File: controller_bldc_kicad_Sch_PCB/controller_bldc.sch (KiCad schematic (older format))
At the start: 57 parts, among them J1 Battery Supply, J2 Emergency Button OUT, J3 Emergency Button IN, J4 Brake, J5 Throttle, J6 LM35, J7 Hall Sensors, J8 Nextion Nx3224T028, J9 BLDC Motor, K1 ADW11, Q1 IRF1010N, Q2 IRF1010N, Q3 IRF1010N, Q4 IRF1010N, Q5 IRF1010N, Q6 IRF1010N, SW1 ON_OFF, SW2 OPC, U1 ESP32-DEVKITC-32D, U2 LM317_TO-220, U3 LM7805_TO220, U4 IR2103, U8 IR2103, U9 IR2103

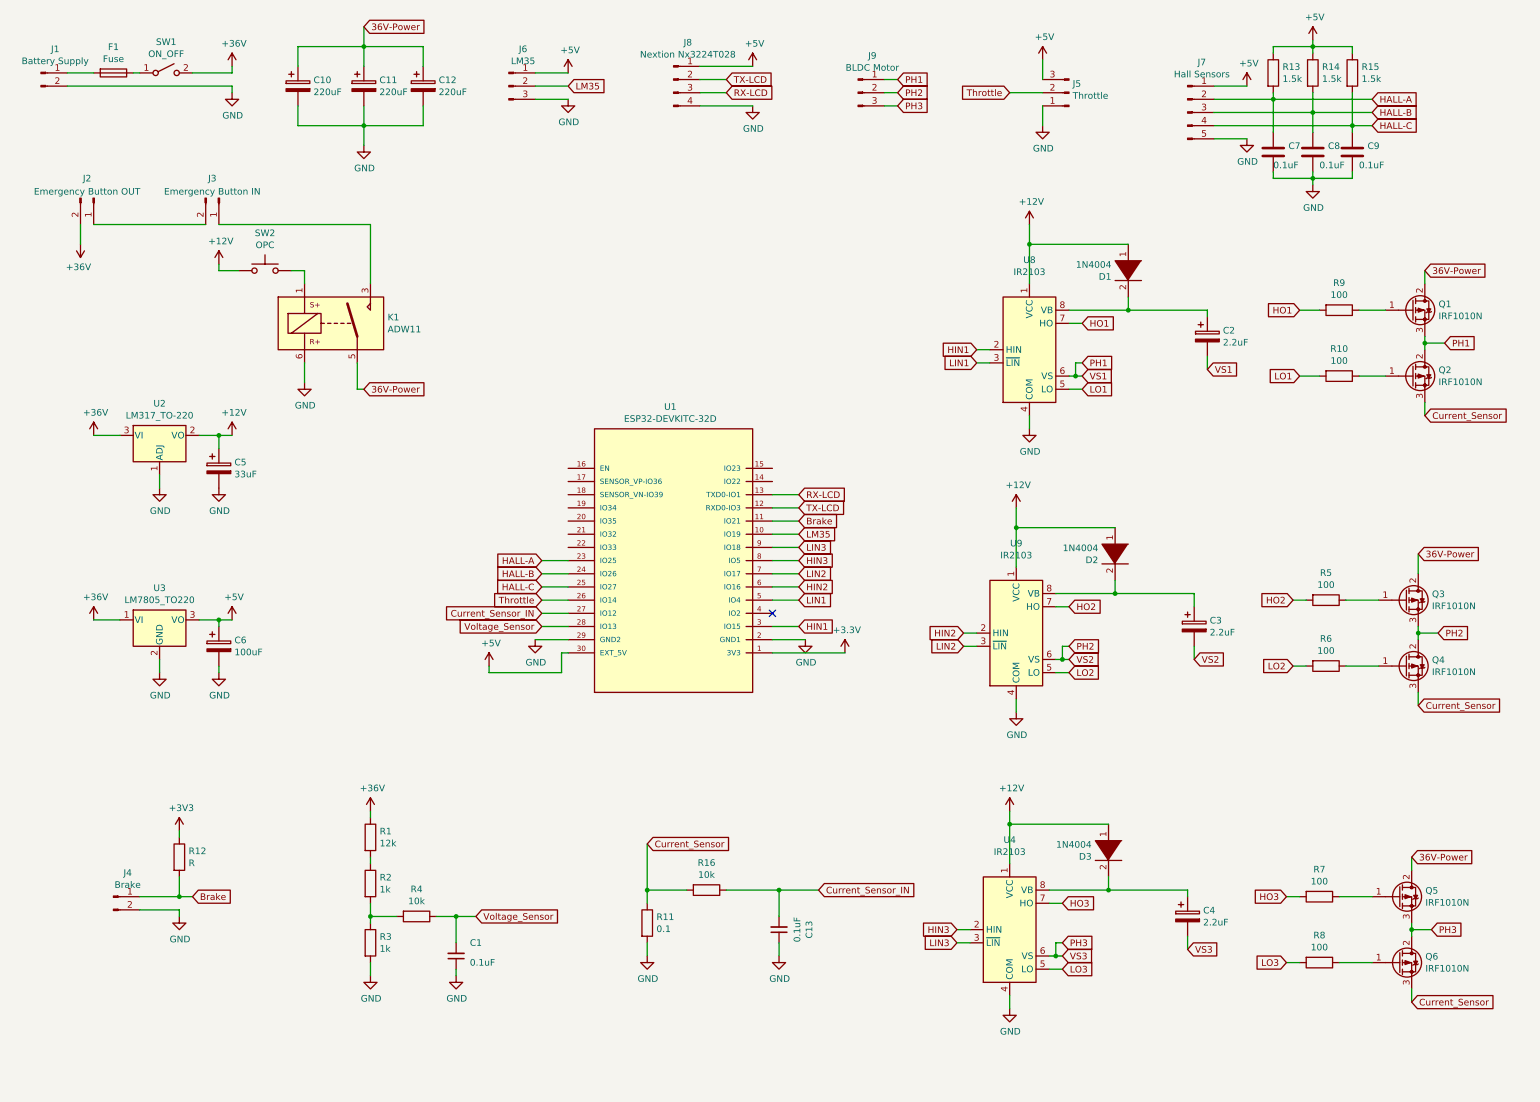
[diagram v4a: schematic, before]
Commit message: PCB: Finished with DC Power Sources and Amp. Op. for sensors
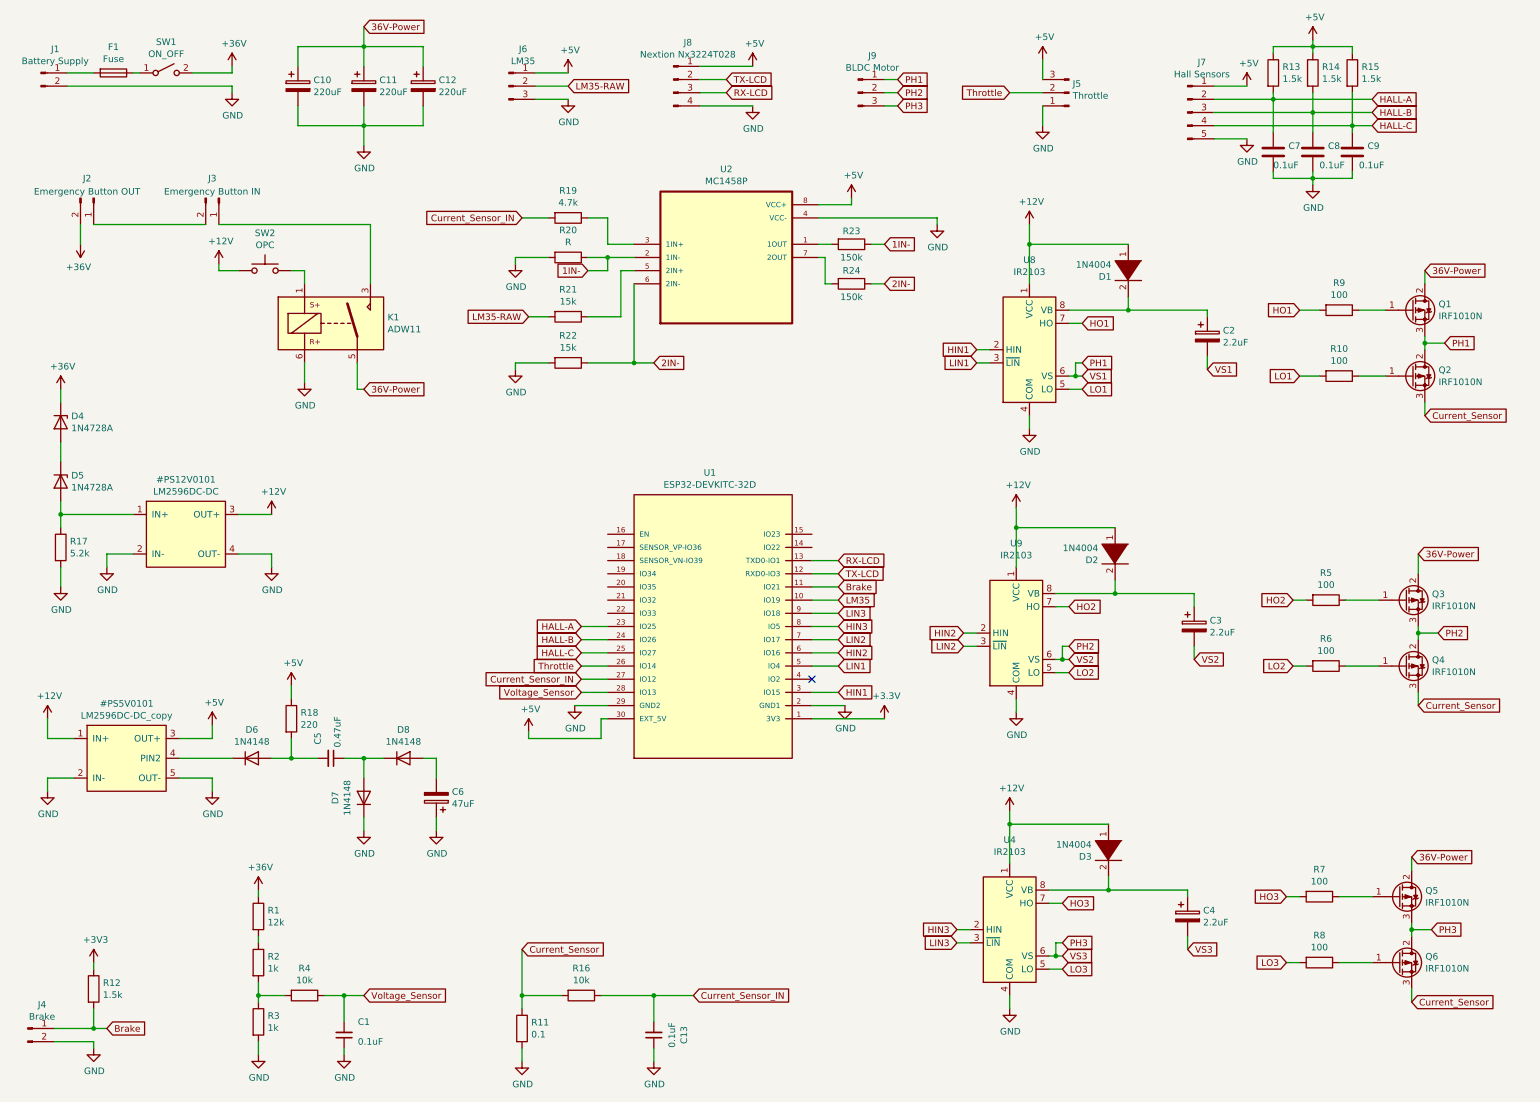
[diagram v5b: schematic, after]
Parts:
- removed C5: 33uF, Capacitor_THT:CP_Radial_D8.0mm_P3.50mm, symbol Device:CP
- removed U2: LM317_TO-220, Package_TO_SOT_THT_Electeam:TO-220-3_Horizontal_TabDown, symbol Regulator_Linear:LM317_TO-220
- removed U3: LM7805_TO220, Package_TO_SOT_THT_Electeam:TO-220-3_Horizontal_TabDown, symbol Regulator_Linear:LM7805_TO220
- added C5: 0.47uF, Capacitor_THT:C_Disc_D7.5mm_W5.0mm_P10.00mm, symbol Device:C_Small
- added D4, D5: 1N4728A, Diode_THT:D_DO-41_SOD81_P10.16mm_Horizontal, symbol Diode:1N47xxA
- added D6, D7, D8: 1N4148, Diode_THT:D_DO-35_SOD27_P7.62mm_Horizontal, symbol Diode:1N4148
- added R17: 5.2k, symbol Device:R
- added R18: 220, symbol Device:R
- added R19: 4.7k, symbol Device:R
- added R20: R, symbol Device:R
- added R21, R22: 15k, symbol Device:R
- added R23, R24: 150k, symbol Device:R
- added U2: MC1458P, DIP794W45P254L959H508Q8, symbol MC1458P:MC1458P
- C6: value 100uF -> 47uF; footprint Capacitor_THT:CP_Radial_D6.3mm_P2.50mm -> (none)
- R12: value R -> 1.5k
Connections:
- net +36V: now also D4.1 (K)
- net +5V: now also R18.1, U2.8 (VCC+); no longer C6.1
- net Current_Sensor_IN: now also R19.2
- net GND: now also C6.1, D7.1 (K), R17.2, R20.2, R22.2, U2.4 (VCC-); no longer C6.2
- net LM35: no longer J6.2 (Pin_2)
- new net: R23.2, U2.1 (1OUT)
- new net: R19.1, U2.3 (1IN+)
- new net: R21.1, U2.5 (2IN+)
- new net: R24.2, U2.7 (2OUT)
- new net: D4.2 (A), D5.1 (K)
- new net: D5.2 (A), R17.1
- new net: C5.1, D7.2 (A), D8.1 (K)
- new net: C6.2, D8.2 (A)
- new net: C5.2, D6.2 (A), R18.2
- new net 1IN-: R20.1, R23.1, U2.2 (1IN-)
- new net 2IN-: R22.1, R24.1, U2.6 (2IN-)
- new net LM35-RAW: J6.2 (Pin_2), R21.2
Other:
- moved on the sheet: C1, C13, J4, R1, R11, R12, R16, R2, R3, R4, U1

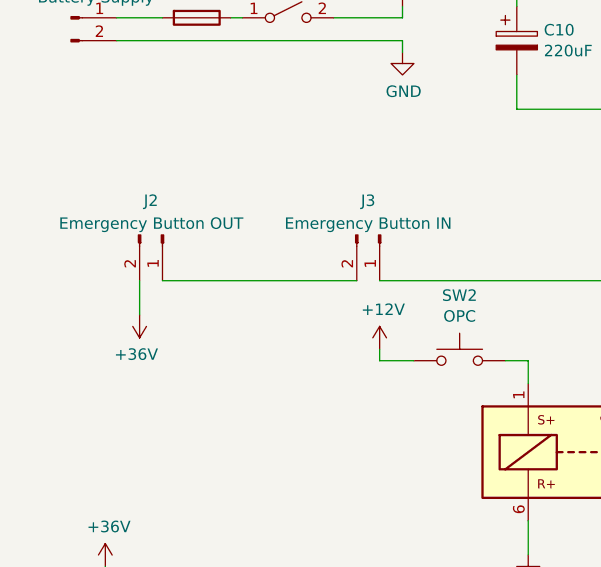
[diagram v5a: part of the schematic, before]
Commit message: PCB: Footprints changed for DC Sources and the OPC realy
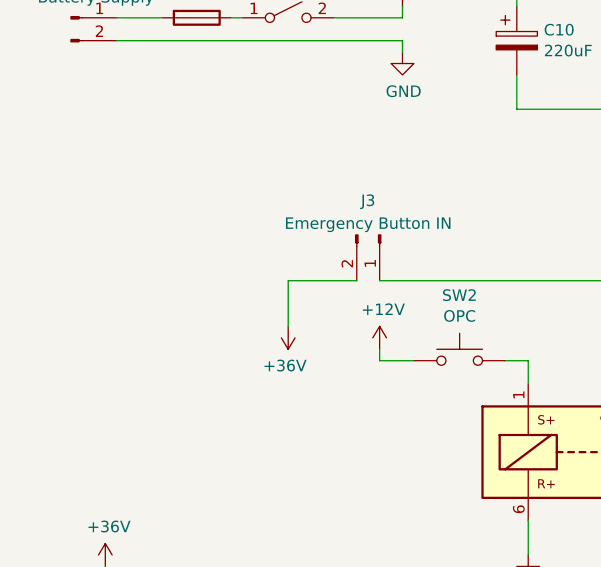
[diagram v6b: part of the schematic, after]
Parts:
- removed J2: Emergency Button OUT, Connector_Phoenix_GMSTB:PhoenixContact_GMSTBA_2,5_2-G_1x02_P7.50mm_Horizontal, symbol Connector:Conn_01x02_Male
- K1: footprint Relay_THT:Relay_1P1T_NO_10x24x18.8mm_Panasonic_ADW11xxxxW_THT -> Relay_THT:Relay_SPDT_RAYEX-L90
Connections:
- net +36V: now also J3.2 (Pin_2)
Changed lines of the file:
@@
 	5350 550  5550 550
-$Comp
-L Connector:Conn_01x02_Male J2
-U 1 1 606A4893
-P 750 1450
-F 0 "J2" V 600 1400 50  0000 C CNN
-F 1 "Emergency Button OUT" V 700 1400 50  0000 C CNN
-F 2 "Connector_Phoenix_GMSTB:PhoenixContact_GMSTBA_2,5_2-G_1x02_P7.50mm_Horizontal" H 750 1450 50  0001 C CNN
-F 3 "~" H 750 1450 50  0001 C CNN
-	1    750  1450
-	0    1    1    0
-$EndComp
 $Comp
 L Connector:Conn_01x02_Male J3
@@
 	0    1    1    0
 $EndComp
-$Comp
-L power:+36V #PWR03
-U 1 1 607E0827
-P 650 1800
-F 0 "#PWR03" H 650 1650 50  0001 C CNN
-F 1 "+36V" H 665 1973 50  0000 C CNN
-F 2 "" H 650 1800 50  0001 C CNN
-F 3 "" H 650 1800 50  0001 C CNN
-	1    650  1800
-	-1   0    0    1
-$EndComp
-Wire Wire Line
-	650  1800 650  1650
-Wire Wire Line
-	750  1650 1600 1650
 Text GLabel 2800 2900 2    50   Input ~ 0
 36V-Power
@@
 F 0 "K1" H 2980 2446 50  0000 L CNN
 F 1 "ADW11" H 2980 2355 50  0000 L CNN
-F 2 "Relay_THT:Relay_1P1T_NO_10x24x18.8mm_Panasonic_ADW11xxxxW_THT" H 3875 2350 50  0001 C CNN
+F 2 "Relay_THT:Relay_SPDT_RAYEX-L90" H 3875 2350 50  0001 C CNN
 F 3 "https://www.panasonic-electric-works.com/pew/es/downloads/ds_dw_hl_en.pdf" H 2550 2400 50  0001 C CNN
 	1    2550 2400
@@
 F 0 "#PS5V0101" H 1000 6115 50  0000 C CNN
 F 1 "LM2596DC-DC_copy" H 1000 6024 50  0000 C CNN
-F 2 "" H 1000 5700 50  0001 C CNN
+F 2 "Package_TO_SOT_THT_Electeam:LM2596DC-DC-HW411" H 1000 5700 50  0001 C CNN
 F 3 "" H 1000 5700 50  0001 C CNN
 	1    1000 5700
@@
 F 0 "#PS12V0101" H 1450 4415 50  0000 C CNN
 F 1 "LM2596DC-DC" H 1450 4324 50  0000 C CNN
-F 2 "" H 1450 4000 50  0001 C CNN
+F 2 "Package_TO_SOT_THT_Electeam:LM2596DC-DC-HW411" H 1450 4000 50  0001 C CNN
 F 3 "" H 1450 4000 50  0001 C CNN
 	1    1450 4000
@@
 Wire Wire Line
 	3950 2700 3950 2750
+$Comp
+L power:+36V #PWR03
+U 1 1 607E0827
+P 1300 1850
+F 0 "#PWR03" H 1300 1700 50  0001 C CNN
+F 1 "+36V" H 1315 2023 50  0000 C CNN
+F 2 "" H 1300 1850 50  0001 C CNN
+F 3 "" H 1300 1850 50  0001 C CNN
+	1    1300 1850
+	-1   0    0    1
+$EndComp
+Wire Wire Line
+	1600 1650 1300 1650
+Wire Wire Line
+	1300 1650 1300 1850
 $EndSCHEMATC

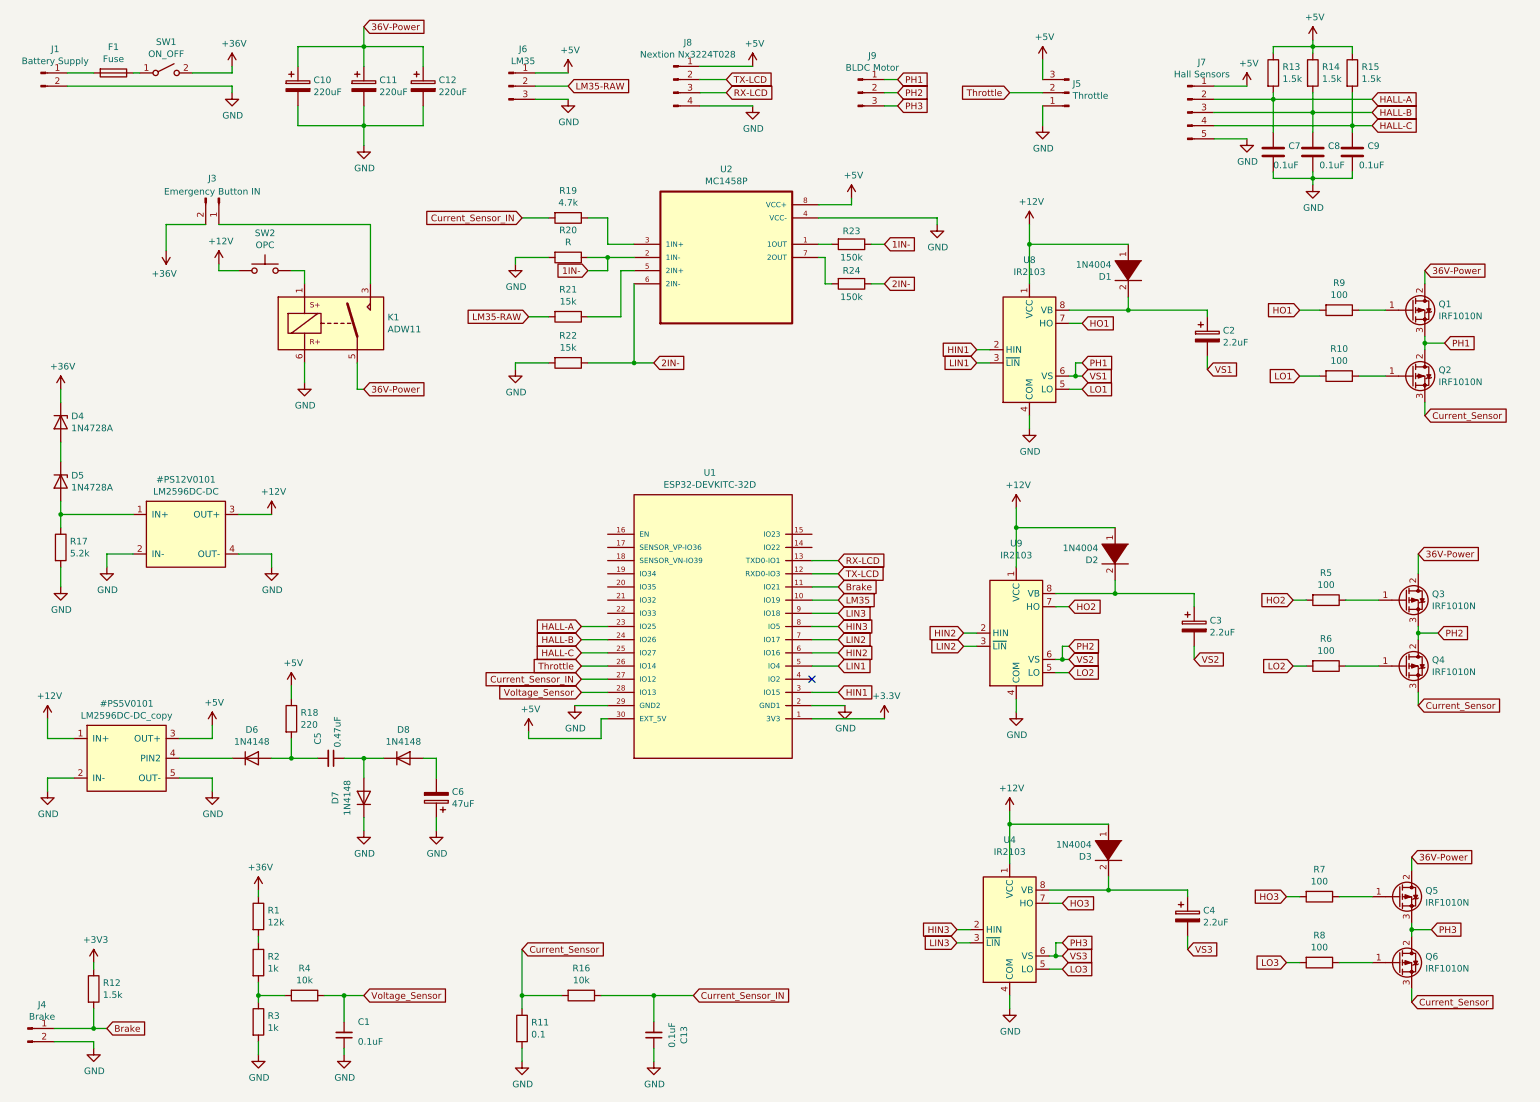
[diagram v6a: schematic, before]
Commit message: This fixes PCB and Schematic, closes #5, closes #6, closes #7, closes #8
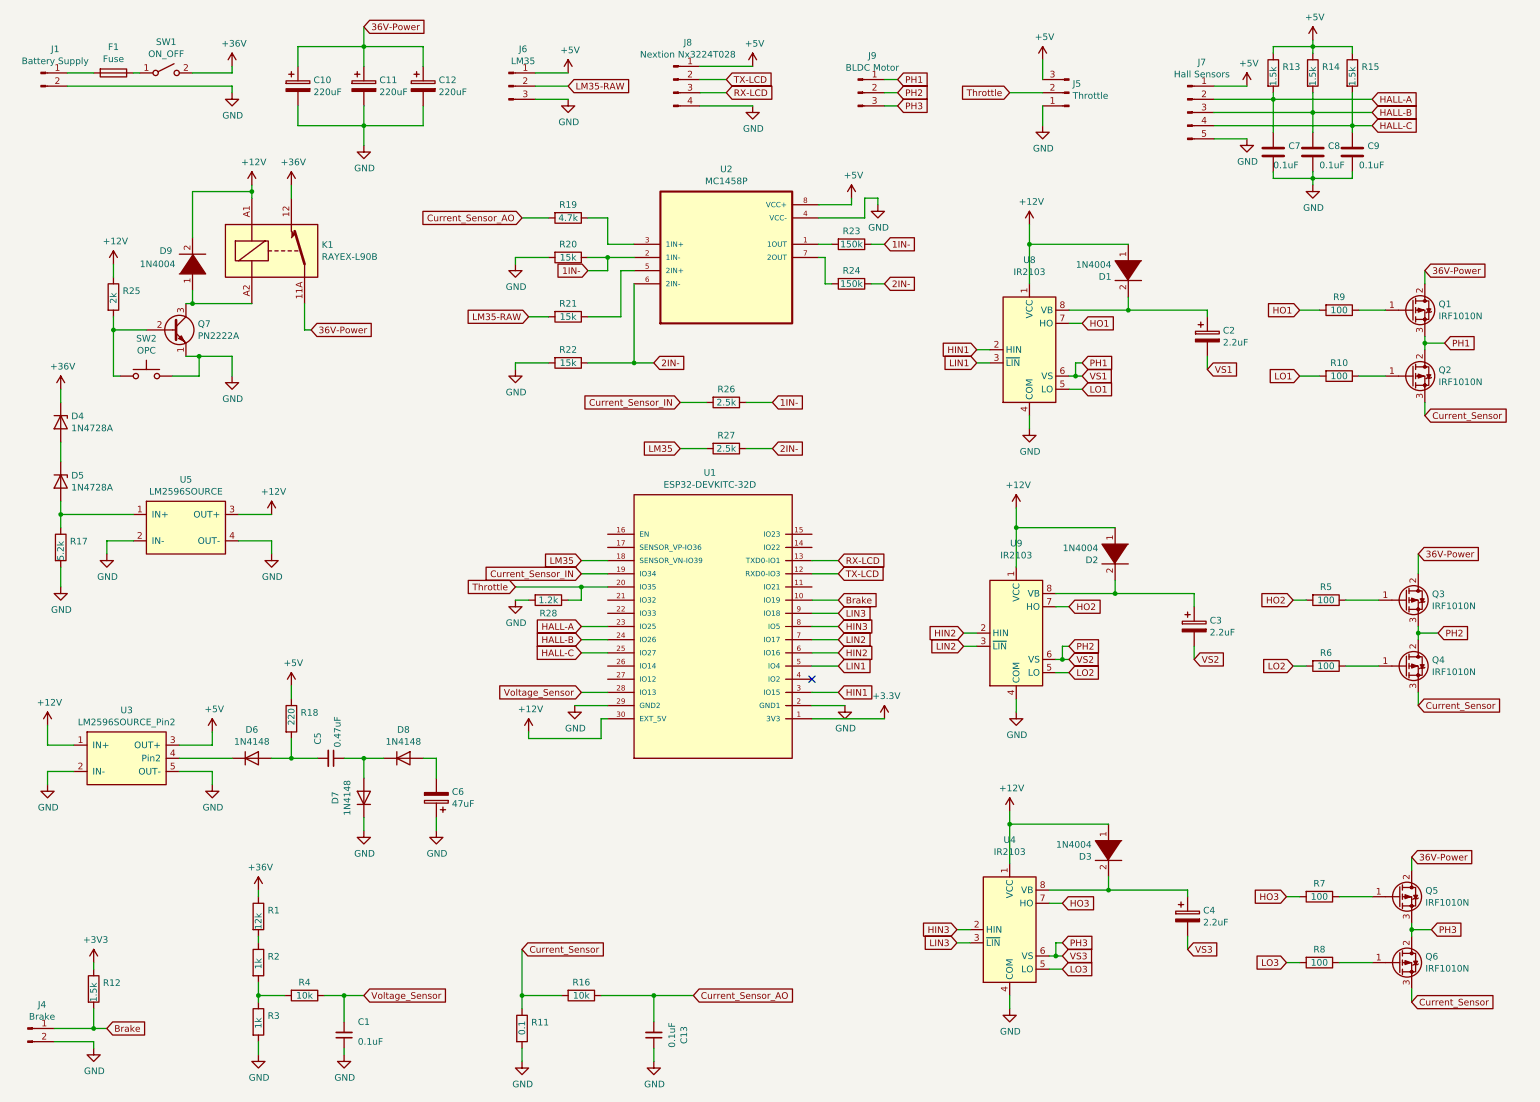
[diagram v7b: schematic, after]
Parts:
- removed J3: Emergency Button IN, Connector_Phoenix_GMSTB:PhoenixContact_GMSTBA_2,5_2-G_1x02_P7.50mm_Horizontal, symbol Connector:Conn_01x02_Male
- removed K1: ADW11, Relay_THT:Relay_SPDT_RAYEX-L90, symbol Relay:ADW11
- added D9: 1N4004, Diode_THT:D_DO-35_SOD27_P7.62mm_Horizontal, symbol pspice:DIODE
- added K1: RAYEX-L90B, Relay_THT:Relay_SPST_RAYEX-L90B, symbol Relay:RAYEX-L90B
- added Q7: PN2222A, Package_TO_SOT_THT:TO-92_Inline, symbol Transistor_BJT:PN2222A
- added R25: 2k, Resistor_THT:R_Axial_DIN0207_L6.3mm_D2.5mm_P10.16mm_Horizontal, symbol Device:R
- added R26, R27: 2.5k, Resistor_THT:R_Axial_DIN0207_L6.3mm_D2.5mm_P10.16mm_Horizontal, symbol Device:R
- added R28: 1.2k, Resistor_THT:R_Axial_DIN0207_L6.3mm_D2.5mm_P10.16mm_Horizontal, symbol Device:R
- added U3: LM2596SOURCE_Pin2, Package_TO_SOT_THT_Electeam:LM2596DCSourcePin2_Electeam, symbol Converter_DCDC_Electeam:LM2596SOURCE_Pin2
- added U5: LM2596SOURCE, Package_TO_SOT_THT_Electeam:LM2596DCSource_Electeam, symbol Converter_DCDC_Electeam:LM2596SOURCE
- C6: footprint (none) -> Capacitor_THT:CP_Radial_D8.0mm_P3.80mm
- R17, R18, R19, R21, R22, R23, R24: footprint (none) -> Resistor_THT:R_Axial_DIN0207_L6.3mm_D2.5mm_P10.16mm_Horizontal
- R20: value R -> 15k; footprint (none) -> Resistor_THT:R_Axial_DIN0207_L6.3mm_D2.5mm_P10.16mm_Horizontal
- U2: footprint DIP794W45P254L959H508Q8 -> Package_DIP:DIP-8_W7.62mm_LongPads
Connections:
- net +12V: now also U1.30 (EXT_5V), D9.2 (A), K1.A1, R25.1, U3.1 (IN+), U5.3 (OUT+); no longer SW2.1
- net +36V: now also K1.12
- net +5V: now also U3.3 (OUT+); no longer U1.30 (EXT_5V)
- net 1IN-: now also R26.1
- net 2IN-: now also R27.1
- net 36V-Power: now also K1.11A, K1.11B
- net Brake: now also U1.10 (IO19); no longer U1.11 (IO21)
- net Current_Sensor_IN: now also U1.19 (IO34), R26.2; no longer C13.2, R16.1, R19.2, U1.27 (IO12)
- net GND: now also SW2.2, Q7.1 (E), R28.2, U3.2 (IN-), U3.5 (OUT-), U5.2 (IN-), U5.4 (OUT-)
- net LM35: now also U1.18 (SENSOR_VN-IO39), R27.2; no longer U1.10 (IO19)
- net Throttle: now also U1.20 (IO35), R28.1; no longer U1.26 (IO14)
- net at D5.2 (A), R17.1: now also U5.1 (IN+)
- net at D6.1 (K): now also U3.4 (Pin2)
- new net: Q7.2 (B), R25.2, SW2.1
- new net: D9.1 (K), K1.A2, Q7.3 (C)
- new net Current_Sensor_AO: C13.2, R16.1, R19.2
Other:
- moved on the sheet: SW2
